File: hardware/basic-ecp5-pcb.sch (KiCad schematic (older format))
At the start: 66 parts, among them J1 Conn_01x02, J2 Conn_02x20_Odd_Even, J3 Conn_02x06_Odd_Even, J4 Conn_02x06_Odd_Even, J5 Conn_02x06_Odd_Even, J6 Conn_02x06_Odd_Even, J7 Conn_02x06_Odd_Even, J8 Conn_02x06_Odd_Even, J9 Conn_02x20_Odd_Even, Q1 Q_NMOS_GSD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

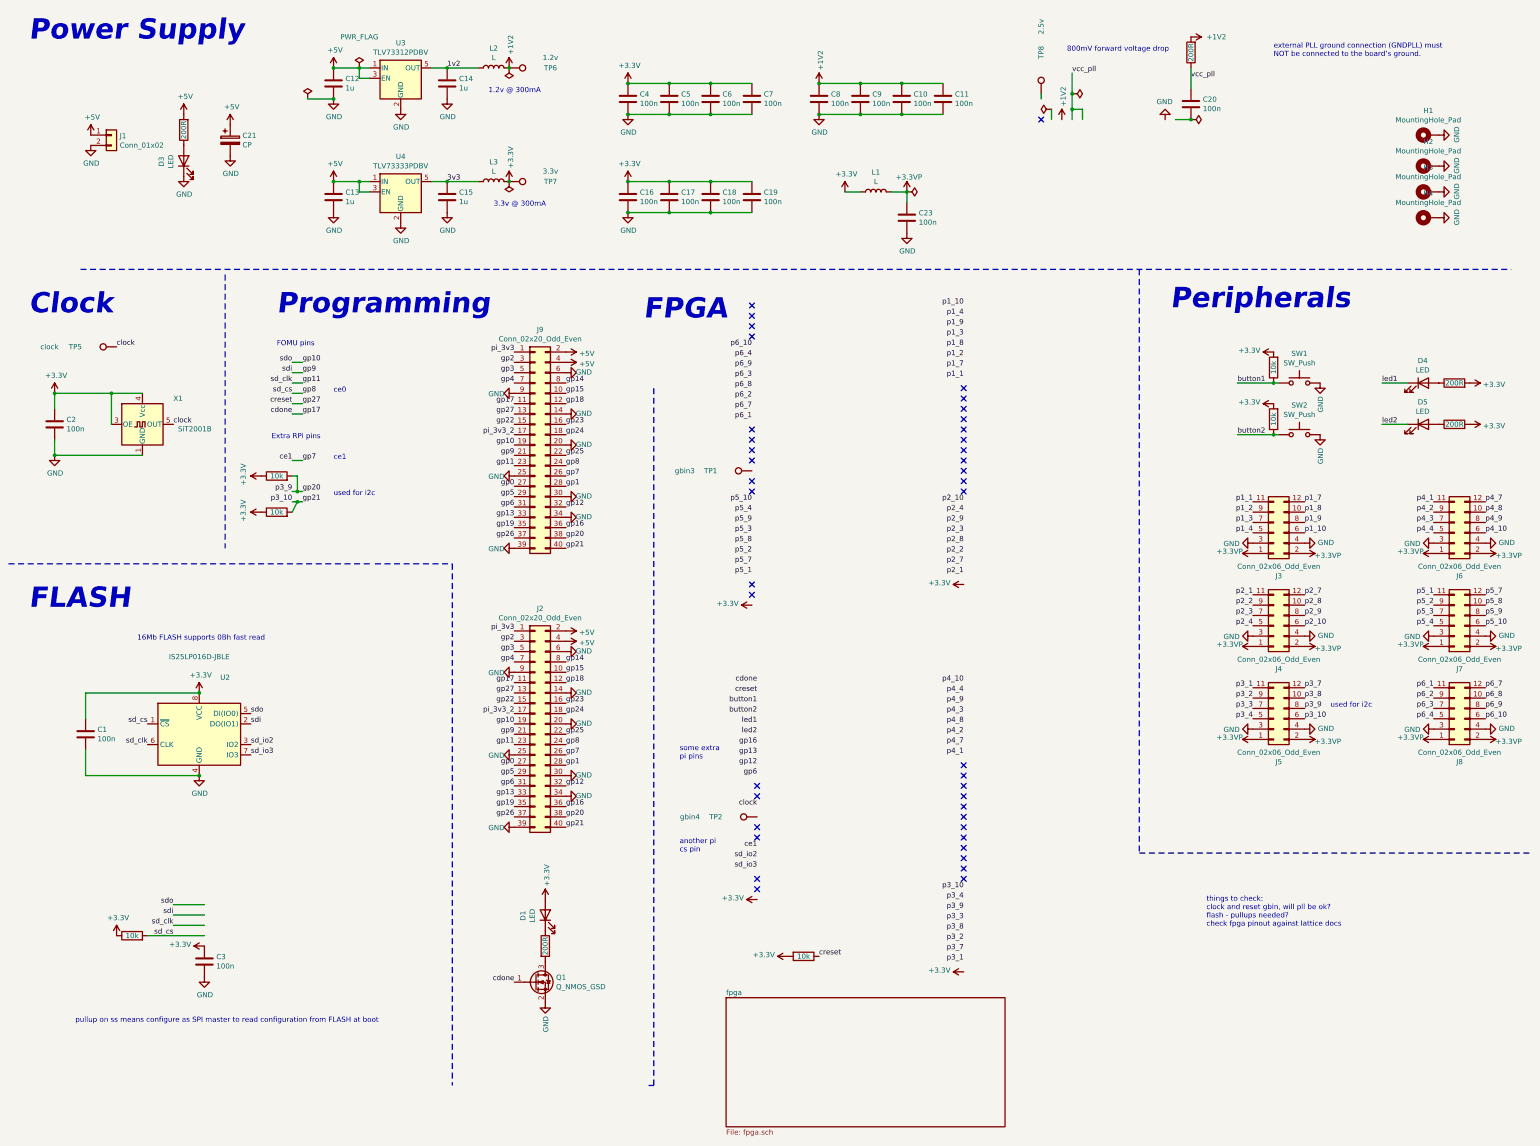
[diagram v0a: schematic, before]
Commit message: pmods connected and routed
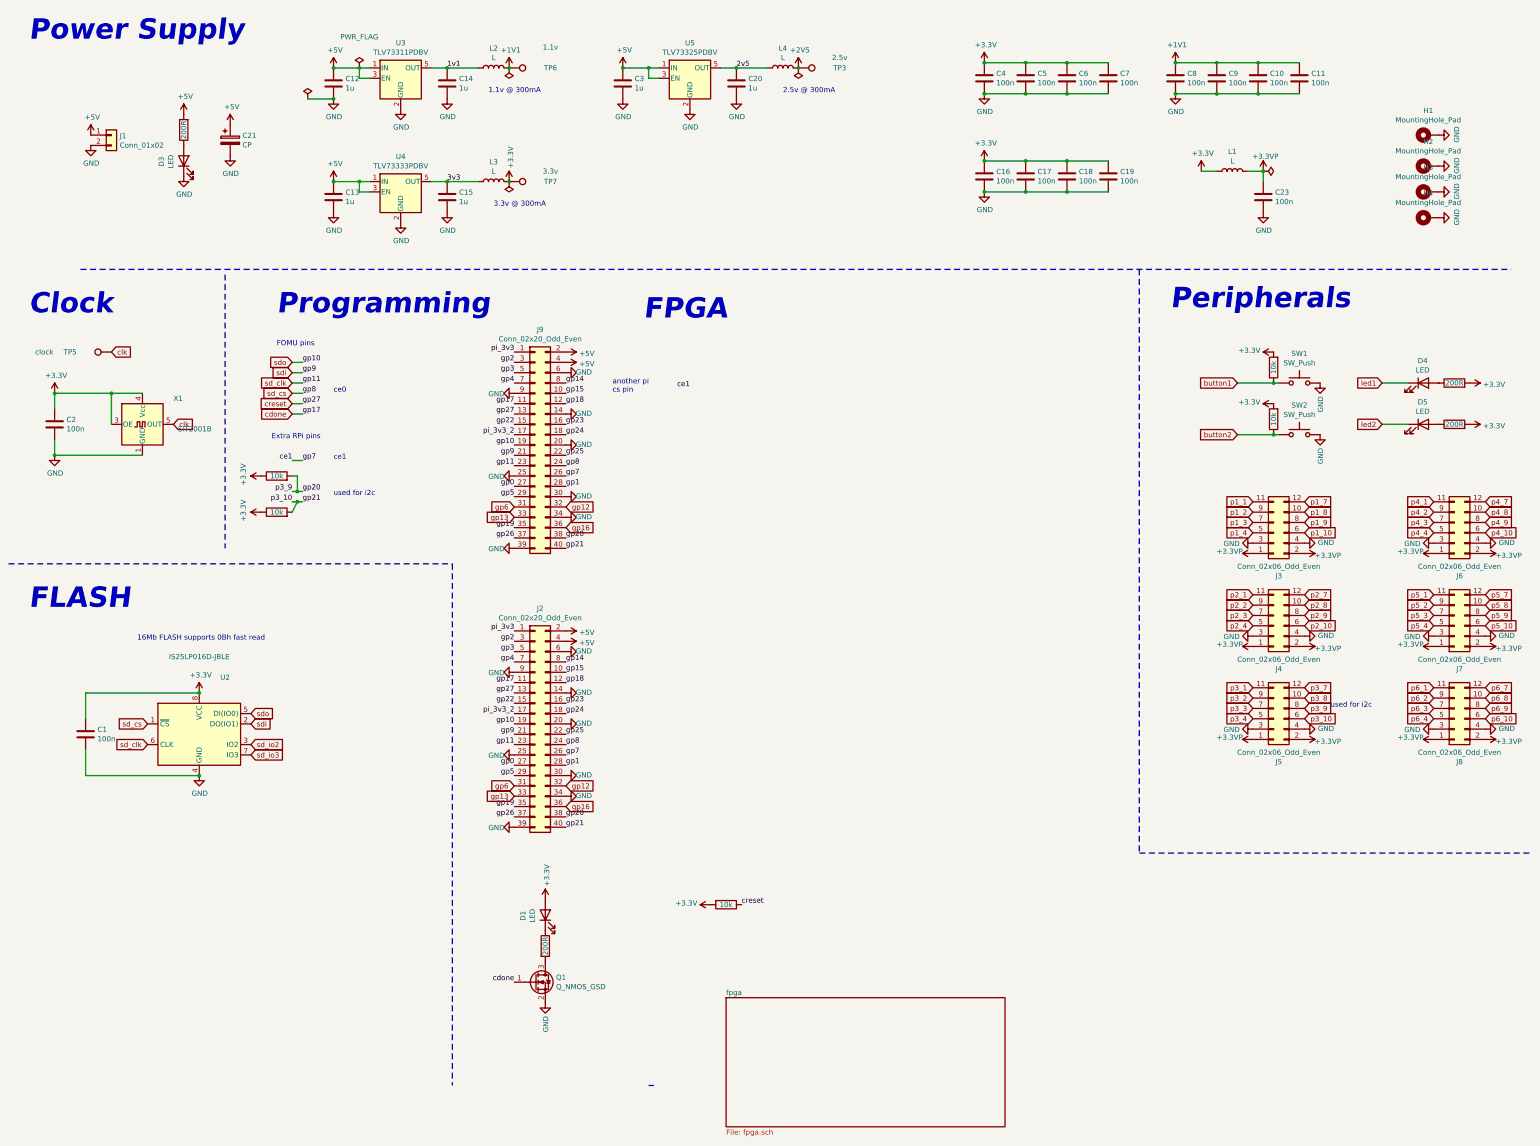
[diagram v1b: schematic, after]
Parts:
- removed R14: 200R, Resistor_SMD:R_0805_2012Metric, symbol Device:R
- removed R4: 10k, Resistor_SMD:R_0805_2012Metric, symbol Device:R
- removed TP1: gbin3, TestPoint:TestPoint_THTPad_D1.0mm_Drill0.5mm, symbol Connector:TestPoint
- removed TP2: gbin4, TestPoint:TestPoint_THTPad_D1.0mm_Drill0.5mm, symbol Connector:TestPoint
- removed TP8: 2.5v, TestPoint:TestPoint_THTPad_D1.0mm_Drill0.5mm, symbol Connector:TestPoint
- added L4: L, Inductor_SMD:L_0805_2012Metric, symbol Device:L
- added TP3: 2.5v, TestPoint:TestPoint_THTPad_D1.0mm_Drill0.5mm, symbol Connector:TestPoint
- added U5: TLV73325PDBV, Package_TO_SOT_SMD:SOT-23-5, symbol Regulator_Linear:TLV73333PDBV
- C20, C3: value 100n -> 1u
- TP6: value 1.2v -> 1.1v
- U3: value TLV73312PDBV -> TLV73311PDBV
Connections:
- net labels added: +1V1, +2V5, 1v1, 2v5, clk
- net labels removed: +1V2, 1v2, clock, vcc_pll
- wire segments 77 -> 70
- no-connect marks 42 -> 0
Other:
- note added: "1.1v @ 300mA"
- note added: "2.5v @ 300mA"
- note removed: "1.2v @ 300mA"
- note removed: "800mV forward voltage drop"
- note removed: "external PLL ground connection (GNDPLL) must\nNOT be connected to the board’s ground."
- note removed: "pullup on ss means configure as SPI master to read configuration from FLASH at boot"
- note removed: "some extra\npi pins"
- note removed: "things to check:\nclock and reset gbin, will pll be ok?\nflash - pullups needed?\ncheck fpga pinout against lattice docs\n\n"
- moved on the sheet: C10, C11, C16, C17, C18, C19, C23, C4, C5, C6, C7, C8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

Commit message: routed
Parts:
- removed C16, C17, C18, C19, C9: 100n, Capacitor_SMD:C_0805_2012Metric, symbol Device:C
- removed R8: 10k, Resistor_SMD:R_0805_2012Metric, symbol Device:R
- added C22, C24, C25, C26: 100n, Capacitor_SMD:C_0805_2012Metric, symbol Device:C
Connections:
- net +2V5: now also C22.1, C24.1, C25.1, C26.1
- net GND: now also C22.2, C24.2, C25.2, C26.2
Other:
- note removed: "ce1"
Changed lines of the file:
@@
 $EndDescr
 $Comp
-L Device:R R8
-U 1 1 5E0BCBC7
-P 7550 9250
-F 0 "R8" V 7343 9250 50  0001 C CNN
-F 1 "10k" V 7550 9250 50  0000 C CNN
-F 2 "Resistor_SMD:R_0805_2012Metric" V 7480 9250 50  0001 C CNN
-F 3 "~" H 7550 9250 50  0001 C CNN
-	1    7550 9250
-	0    1    1    0
-$EndComp
-$Comp
-L power:+3.3V #PWR0101
-U 1 1 5E0BE64B
-P 7400 9250
-F 0 "#PWR0101" H 7400 9100 50  0001 C CNN
-F 1 "+3.3V" V 7415 9378 50  0000 L CNN
-F 2 "" H 7400 9250 50  0001 C CNN
-F 3 "" H 7400 9250 50  0001 C CNN
-	1    7400 9250
-	0    -1   -1   0
-$EndComp
-$Comp
 L Device:LED D1
 U 1 1 5E0C043C
@@
 $EndComp
 $Comp
-L Device:C C9
-U 1 1 5E0E0BDD
-P 12300 1250
-F 0 "C9" H 12415 1296 50  0000 L CNN
-F 1 "100n" H 12415 1205 50  0000 L CNN
-F 2 "Capacitor_SMD:C_0805_2012Metric" H 12338 1100 50  0001 C CNN
-F 3 "~" H 12300 1250 50  0001 C CNN
-	1    12300 1250
-	1    0    0    -1
-$EndComp
-$Comp
 L Device:C C10
 U 1 1 5E0E1158
@@
 $EndComp
 Wire Wire Line
-	11900 1100 12300 1100
-Wire Wire Line
-	12300 1100 12700 1100
-Connection ~ 12300 1100
-Wire Wire Line
 	12700 1100 13100 1100
 Connection ~ 12700 1100
 Wire Wire Line
 	13100 1400 12700 1400
-Wire Wire Line
-	12700 1400 12300 1400
 Connection ~ 12700 1400
-Wire Wire Line
-	12300 1400 11900 1400
-Connection ~ 12300 1400
 Connection ~ 11900 1400
 $Comp
@@
 	1    0    0    -1
 $EndComp
-Text Label 7700 9250 0    50   ~ 0
-creset
 Wire Wire Line
 	12500 4200 12850 4200
@@
 Wire Notes Line
 	4100 5950 600  5950
-$Comp
-L power:+3.3V #PWR01
-U 1 1 5E72131E
-P 10050 2050
-F 0 "#PWR01" H 10050 1900 50  0001 C CNN
-F 1 "+3.3V" H 10065 2223 50  0000 C CNN
-F 2 "" H 10050 2050 50  0001 C CNN
-F 3 "" H 10050 2050 50  0001 C CNN
-	1    10050 2050
-	1    0    0    -1
-$EndComp
-$Comp
-L power:GND #PWR02
-U 1 1 5E721328
-P 10050 2350
-F 0 "#PWR02" H 10050 2100 50  0001 C CNN
-F 1 "GND" H 10055 2177 50  0000 C CNN
-F 2 "" H 10050 2350 50  0001 C CNN
-F 3 "" H 10050 2350 50  0001 C CNN
-	1    10050 2350
-	1    0    0    -1
-$EndComp
-$Comp
-L Device:C C16
-U 1 1 5E721332
-P 10050 2200
-F 0 "C16" H 10165 2246 50  0000 L CNN
-F 1 "100n" H 10165 2155 50  0000 L CNN
-F 2 "Capacitor_SMD:C_0805_2012Metric" H 10088 2050 50  0001 C CNN
-F 3 "~" H 10050 2200 50  0001 C CNN
-	1    10050 2200
-	1    0    0    -1
-$EndComp
-$Comp
-L Device:C C17
-U 1 1 5E72133C
-P 10450 2200
-F 0 "C17" H 10565 2246 50  0000 L CNN
-F 1 "100n" H 10565 2155 50  0000 L CNN
-F 2 "Capacitor_SMD:C_0805_2012Metric" H 10488 2050 50  0001 C CNN
-F 3 "~" H 10450 2200 50  0001 C CNN
-	1    10450 2200
-	1    0    0    -1
-$EndComp
-$Comp
-L Device:C C18
-U 1 1 5E721346
-P 10850 2200
-F 0 "C18" H 10965 2246 50  0000 L CNN
-F 1 "100n" H 10965 2155 50  0000 L CNN
-F 2 "Capacitor_SMD:C_0805_2012Metric" H 10888 2050 50  0001 C CNN
-F 3 "~" H 10850 2200 50  0001 C CNN
-	1    10850 2200
-	1    0    0    -1
-$EndComp
-$Comp
-L Device:C C19
-U 1 1 5E721350
-P 11250 2200
-F 0 "C19" H 11365 2246 50  0000 L CNN
-F 1 "100n" H 11365 2155 50  0000 L CNN
-F 2 "Capacitor_SMD:C_0805_2012Metric" H 11288 2050 50  0001 C CNN
-F 3 "~" H 11250 2200 50  0001 C CNN
-	1    11250 2200
-	1    0    0    -1
-$EndComp
-Wire Wire Line
-	10050 2050 10450 2050
-Connection ~ 10050 2050
-Wire Wire Line
-	10450 2050 10850 2050
-Connection ~ 10450 2050
-Wire Wire Line
-	10850 2050 11250 2050
-Connection ~ 10850 2050
-Wire Wire Line
-	11250 2350 10850 2350
-Wire Wire Line
-	10850 2350 10450 2350
-Connection ~ 10850 2350
-Wire Wire Line
-	10450 2350 10050 2350
-Connection ~ 10450 2350
-Connection ~ 10050 2350
 Text Label 5500 10000 2    50   ~ 0
 cdone
@@
 Text Label 3450 4950 0    50   ~ 0
 gp7
-Text Notes 3750 4950 0    50   ~ 0
-ce1
 Text Notes 3750 4300 0    50   ~ 0
 ce0
@@
 	0    -1   -1   0
 $EndComp
-Text Label 3350 4950 2    50   ~ 0
-ce1
 Wire Wire Line
 	3350 4950 3450 4950
-Text Label 7200 4250 2    50   ~ 0
-ce1
 Text Notes 3150 4750 0    50   ~ 0
 Extra RPi pins
 Text Notes 13400 7350 0    50   ~ 0
 used for i2c
-Text Notes 6450 4300 0    50   ~ 0
+Text Notes 3750 5000 0    50   ~ 0
 another pi\ncs pin
 $Sheet
-S 7550 10150 2700 1250
+S 7550 5550 2700 1250
 U 5F109712
 F0 "fpga" 50
@@
 Text GLabel 6000 5600 2    50   Input ~ 0
 gp16
+$Comp
+L power:GND #PWR0104
+U 1 1 5F21B101
+P 10050 2200
+F 0 "#PWR0104" H 10050 1950 50  0001 C CNN
+F 1 "GND" H 10055 2027 50  0000 C CNN
+F 2 "" H 10050 2200 50  0001 C CNN
+F 3 "" H 10050 2200 50  0001 C CNN
+	1    10050 2200
+	1    0    0    -1
+$EndComp
+$Comp
+L Device:C C22
+U 1 1 5F21B107
+P 10050 2050
+F 0 "C22" H 10165 2096 50  0000 L CNN
+F 1 "100n" H 10165 2005 50  0000 L CNN
+F 2 "Capacitor_SMD:C_0805_2012Metric" H 10088 1900 50  0001 C CNN
+F 3 "~" H 10050 2050 50  0001 C CNN
+	1    10050 2050
+	1    0    0    -1
+$EndComp
+$Comp
+L Device:C C24
+U 1 1 5F21B10D
+P 10450 2050
+F 0 "C24" H 10565 2096 50  0000 L CNN
+F 1 "100n" H 10565 2005 50  0000 L CNN
+F 2 "Capacitor_SMD:C_0805_2012Metric" H 10488 1900 50  0001 C CNN
+F 3 "~" H 10450 2050 50  0001 C CNN
+	1    10450 2050
+	1    0    0    -1
+$EndComp
+$Comp
+L Device:C C25
+U 1 1 5F21B113
+P 10850 2050
+F 0 "C25" H 10965 2096 50  0000 L CNN
+F 1 "100n" H 10965 2005 50  0000 L CNN
+F 2 "Capacitor_SMD:C_0805_2012Metric" H 10888 1900 50  0001 C CNN
+F 3 "~" H 10850 2050 50  0001 C CNN
+	1    10850 2050
+	1    0    0    -1
+$EndComp
+$Comp
+L Device:C C26
+U 1 1 5F21B119
+P 11250 2050
+F 0 "C26" H 11365 2096 50  0000 L CNN
+F 1 "100n" H 11365 2005 50  0000 L CNN
+F 2 "Capacitor_SMD:C_0805_2012Metric" H 11288 1900 50  0001 C CNN
+F 3 "~" H 11250 2050 50  0001 C CNN
+	1    11250 2050
+	1    0    0    -1
+$EndComp
+Wire Wire Line
+	10050 1900 10450 1900
+Wire Wire Line
+	10450 1900 10850 1900
+Connection ~ 10450 1900
+Wire Wire Line
+	10850 1900 11250 1900
+Connection ~ 10850 1900
+Wire Wire Line
+	11250 2200 10850 2200
+Wire Wire Line
+	10850 2200 10450 2200
+Connection ~ 10850 2200
+Wire Wire Line
+	10450 2200 10050 2200
+Connection ~ 10450 2200
+Connection ~ 10050 2200
+$Comp
+L power:+2V5 #PWR0105
+U 1 1 5F21EACD
+P 10050 1900
+F 0 "#PWR0105" H 10050 1750 50  0001 C CNN
+F 1 "+2V5" H 10065 2073 50  0000 C CNN
+F 2 "" H 10050 1900 50  0001 C CNN
+F 3 "" H 10050 1900 50  0001 C CNN
+	1    10050 1900
+	1    0    0    -1
+$EndComp
+Connection ~ 10050 1900
+Wire Wire Line
+	11900 1100 12700 1100
+Wire Wire Line
+	11900 1400 12700 1400
+Text GLabel 3350 4950 0    50   Input ~ 0
+ce1
 $EndSCHEMATC
